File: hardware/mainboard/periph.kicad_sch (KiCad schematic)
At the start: 64 parts

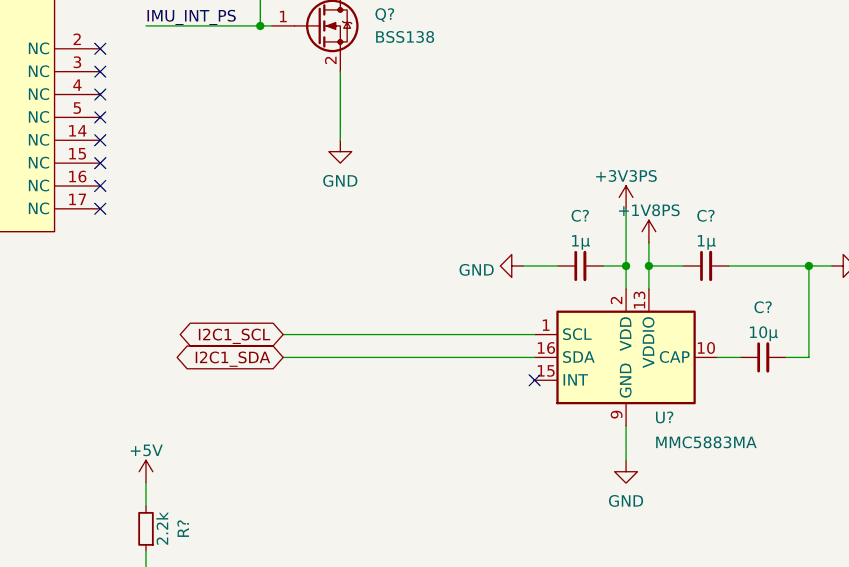
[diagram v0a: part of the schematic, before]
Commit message: Re-add USB-C PD control
Signed-off-by: gatecat <gatecat@ds0.me>
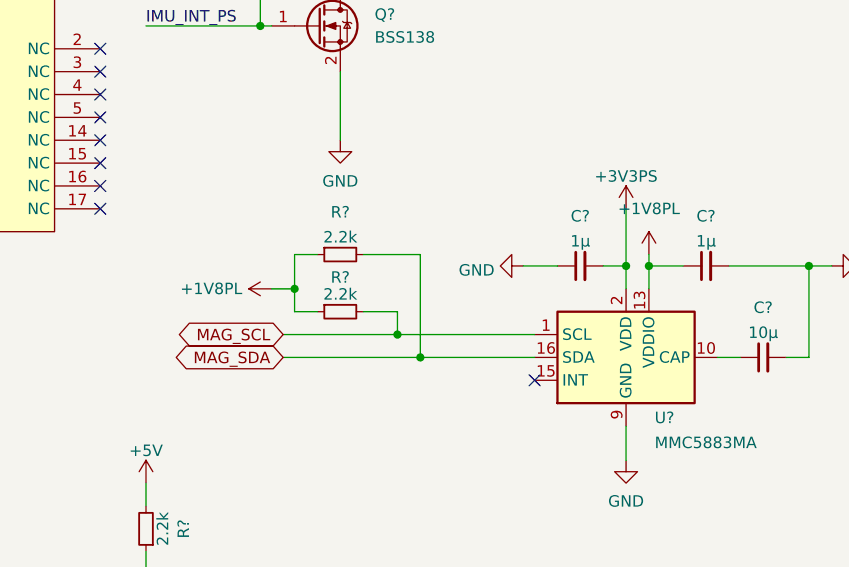
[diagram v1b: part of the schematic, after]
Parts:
- added R? (x2): 2.2k, Resistor_SMD:R_0402_1005Metric, symbol Device:R_Small
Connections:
- net +1V8PL: now also C?.1, U?.13 (VDDIO), R?.1, R?.1
- net +1V8PS: no longer C?.1, U?.13 (VDDIO)
- net I2C1_SCL: no longer U?.1 (SCL)
- net I2C1_SDA: no longer U?.16 (SDA)
- new net MAG_SCL: R?.2, U?.1 (SCL)
- new net MAG_SDA: R?.2, U?.16 (SDA)
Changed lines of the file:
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@@
   (junction (at 201.93 158.75) (diameter 0) (color 0 0 0 0)
   )
+  (junction (at 144.78 161.29) (diameter 0) (color 0 0 0 0)
+  )
   (junction (at 337.82 114.3) (diameter 0) (color 0 0 0 0)
   )
@@
   (junction (at 337.82 152.4) (diameter 0) (color 0 0 0 0)
   )
+  (junction (at 158.75 168.91) (diameter 0) (color 0 0 0 0)
+  )
   (junction (at 88.9 102.87) (diameter 0) (color 0 0 0 0)
   )
@@
   )
   (junction (at 233.68 140.97) (diameter 0) (color 0 0 0 0)
+  )
+  (junction (at 156.21 166.37) (diameter 0) (color 0 0 0 0)
   )
   (junction (at 391.16 66.04) (diameter 0) (color 0 0 0 0)
@@
     (stroke (width 0) (type default) (color 0 0 0 0))
   )
+  (wire (pts (xy 158.75 168.91) (xy 171.45 168.91))
+    (stroke (width 0) (type default) (color 0 0 0 0))
+  )
   (wire (pts (xy 176.53 45.72) (xy 190.5 45.72))
     (stroke (width 0) (type default) (color 0 0 0 0))
@@
     (stroke (width 0) (type default) (color 0 0 0 0))
   )
-  (wire (pts (xy 184.15 156.21) (xy 184.15 158.75))
+  (wire (pts (xy 184.15 157.48) (xy 184.15 158.75))
     (stroke (width 0) (type default) (color 0 0 0 0))
   )
@@
     (stroke (width 0) (type default) (color 0 0 0 0))
   )
+  (wire (pts (xy 156.21 166.37) (xy 171.45 166.37))
+    (stroke (width 0) (type default) (color 0 0 0 0))
+  )
   (wire (pts (xy 86.36 215.9) (xy 86.36 220.98))
     (stroke (width 0) (type default) (color 0 0 0 0))
@@
     (stroke (width 0) (type default) (color 0 0 0 0))
   )
+  (wire (pts (xy 144.78 161.29) (xy 144.78 157.48))
+    (stroke (width 0) (type default) (color 0 0 0 0))
+  )
   (wire (pts (xy 69.85 102.87) (xy 69.85 105.41))
     (stroke (width 0) (type default) (color 0 0 0 0))
@@
     (stroke (width 0) (type default) (color 0 0 0 0))
   )
+  (wire (pts (xy 152.4 157.48) (xy 158.75 157.48))
+    (stroke (width 0) (type default) (color 0 0 0 0))
+  )
   (wire (pts (xy 391.16 68.58) (xy 391.16 147.32))
     (stroke (width 0) (type default) (color 0 0 0 0))
@@
     (stroke (width 0) (type default) (color 0 0 0 0))
   )
-  (wire (pts (xy 143.51 168.91) (xy 171.45 168.91))
+  (wire (pts (xy 143.51 168.91) (xy 158.75 168.91))
     (stroke (width 0) (type default) (color 0 0 0 0))
   )
@@
     (stroke (width 0) (type default) (color 0 0 0 0))
   )
-  (wire (pts (xy 143.51 166.37) (xy 171.45 166.37))
+  (wire (pts (xy 143.51 166.37) (xy 156.21 166.37))
     (stroke (width 0) (type default) (color 0 0 0 0))
   )
@@
     (stroke (width 0) (type default) (color 0 0 0 0))
   )
+  (wire (pts (xy 152.4 163.83) (xy 156.21 163.83))
+    (stroke (width 0) (type default) (color 0 0 0 0))
+  )
   (wire (pts (xy 66.04 127) (xy 92.71 127))
     (stroke (width 0) (type default) (color 0 0 0 0))
@@
     (stroke (width 0) (type default) (color 0 0 0 0))
   )
+  (wire (pts (xy 144.78 161.29) (xy 144.78 163.83))
+    (stroke (width 0) (type default) (color 0 0 0 0))
+  )
   (wire (pts (xy 306.07 139.7) (xy 309.88 139.7))
     (stroke (width 0) (type default) (color 0 0 0 0))
@@
     (stroke (width 0) (type default) (color 0 0 0 0))
   )
+  (wire (pts (xy 156.21 163.83) (xy 156.21 166.37))
+    (stroke (width 0) (type default) (color 0 0 0 0))
+  )
   (wire (pts (xy 55.88 264.16) (xy 55.88 261.62))
     (stroke (width 0) (type default) (color 0 0 0 0))
@@
     (stroke (width 0) (type default) (color 0 0 0 0))
   )
+  (wire (pts (xy 142.24 161.29) (xy 144.78 161.29))
+    (stroke (width 0) (type default) (color 0 0 0 0))
+  )
   (wire (pts (xy 363.22 163.83) (xy 363.22 166.37))
     (stroke (width 0) (type default) (color 0 0 0 0))
@@
     (stroke (width 0) (type default) (color 0 0 0 0))
   )
+  (wire (pts (xy 144.78 163.83) (xy 147.32 163.83))
+    (stroke (width 0) (type default) (color 0 0 0 0))
+  )
   (wire (pts (xy 132.08 22.86) (xy 140.97 22.86))
     (stroke (width 0) (type default) (color 0 0 0 0))
@@
     (stroke (width 0) (type default) (color 0 0 0 0))
   )
+  (wire (pts (xy 158.75 157.48) (xy 158.75 168.91))
+    (stroke (width 0) (type default) (color 0 0 0 0))
+  )
   (wire (pts (xy 140.97 31.75) (xy 140.97 33.02))
     (stroke (width 0) (type default) (color 0 0 0 0))
@@
   )
   (wire (pts (xy 209.55 140.97) (xy 218.44 140.97))
+    (stroke (width 0) (type default) (color 0 0 0 0))
+  )
+  (wire (pts (xy 144.78 157.48) (xy 147.32 157.48))
     (stroke (width 0) (type default) (color 0 0 0 0))
   )
@@
     )
   )
-  (global_label "I2C1_SDA" (shape bidirectional) (at 143.51 168.91 180) (fields_autoplaced)
+  (global_label "MAG_SDA" (shape bidirectional) (at 143.51 168.91 180) (fields_autoplaced)
     (effects (font (size 1.27 1.27)) (justify right))
-    (property "Intersheet References" "${INTERSHEET_REFS}" (id 0) (at 132.2674 168.8306 0)
+    (property "Intersheet References" "${INTERSHEET_REFS}" (id 0) (at 132.7512 168.8306 0)
       (effects (font (size 1.27 1.27)) (justify right) hide)
     )
   )
-  (global_label "I2C1_SCL" (shape bidirectional) (at 143.51 166.37 180) (fields_autoplaced)
+  (global_label "MAG_SCL" (shape bidirectional) (at 143.51 166.37 180) (fields_autoplaced)
     (effects (font (size 1.27 1.27)) (justify right))
-    (property "Intersheet References" "${INTERSHEET_REFS}" (id 0) (at 132.3279 166.2906 0)
+    (property "Intersheet References" "${INTERSHEET_REFS}" (id 0) (at 132.8117 166.2906 0)
       (effects (font (size 1.27 1.27)) (justify right) hide)
     )
@@
     (pin "2")
   )
+  (symbol (lib_id "meowality:+1V8PL") (at 184.15 157.48 0) (unit 1)
+    (in_bom yes) (on_board yes) (fields_autoplaced)
+    (property "Reference" "#PWR?" (id 0) (at 184.15 161.29 0)
+      (effects (font (size 1.27 1.27)) hide)
+    )
+    (property "Value" "+1V8PL" (id 1) (at 184.15 152.4 0))
+    (property "Footprint" "" (id 2) (at 184.15 157.48 0)
+      (effects (font (size 1.27 1.27)) hide)
+    )
+    (property "Datasheet" "" (id 3) (at 184.15 157.48 0)
+      (effects (font (size 1.27 1.27)) hide)
+    )
+    (pin "1")
+  )
   (symbol (lib_id "Device:C_Small") (at 312.42 139.7 90) (unit 1)
     (in_bom yes) (on_board yes)
@@
     (pin "2")
   )
+  (symbol (lib_id "meowality:+1V8PL") (at 142.24 161.29 90) (unit 1)
+    (in_bom yes) (on_board yes)
+    (property "Reference" "#PWR?" (id 0) (at 146.05 161.29 0)
+      (effects (font (size 1.27 1.27)) hide)
+    )
+    (property "Value" "+1V8PL" (id 1) (at 132.08 161.29 90)
+      (effects (font (size 1.27 1.27)) (justify right))
+    )
+    (property "Footprint" "" (id 2) (at 142.24 161.29 0)
+      (effects (font (size 1.27 1.27)) hide)
+    )
+    (property "Datasheet" "" (id 3) (at 142.24 161.29 0)
+      (effects (font (size 1.27 1.27)) hide)
+    )
+    (pin "1")
+  )
   (symbol (lib_id "Device:C_Small") (at 209.55 124.46 0) (unit 1)
     (in_bom yes) (on_board yes)
@@
     (pin "3")
     (pin "4")
+  )
+  (symbol (lib_id "Device:R_Small") (at 149.86 163.83 90) (mirror x) (unit 1)
+    (in_bom yes) (on_board yes)
+    (property "Reference" "R?" (id 0) (at 149.86 160.02 90))
+    (property "Value" "2.2k" (id 1) (at 149.86 161.902 90))
+    (property "Footprint" "Resistor_SMD:R_0402_1005Metric" (id 2) (at 149.86 163.83 0)
+      (effects (font (size 1.27 1.27)) hide)
+    )
+    (property "Datasheet" "~" (id 3) (at 149.86 163.83 0)
+      (effects (font (size 1.27 1.27)) hide)
+    )
+    (pin "1")
+    (pin "2")
   )
   (symbol (lib_id "power:GND") (at 138.43 269.24 0) (unit 1)
@@
     (pin "2")
   )
+  (symbol (lib_id "Device:R_Small") (at 149.86 157.48 90) (mirror x) (unit 1)
+    (in_bom yes) (on_board yes) (fields_autoplaced)
+    (property "Reference" "R?" (id 0) (at 149.86 152.7769 90))
+    (property "Value" "2.2k" (id 1) (at 149.86 155.552 90))
+    (property "Footprint" "Resistor_SMD:R_0402_1005Metric" (id 2) (at 149.86 157.48 0)
+      (effects (font (size 1.27 1.27)) hide)
+    )
+    (property "Datasheet" "~" (id 3) (at 149.86 157.48 0)
+      (effects (font (size 1.27 1.27)) hide)
+    )
+    (pin "1")
+    (pin "2")
+  )
   (symbol (lib_id "Transistor_FET:BSS138") (at 83.82 205.74 0) (unit 1)
     (in_bom yes) (on_board yes) (fields_autoplaced)
@@
     (pin "2")
   )
-  (symbol (lib_id "meowality:+1V8PS") (at 184.15 156.21 0) (unit 1)
-    (in_bom yes) (on_board yes) (fields_autoplaced)
-    (property "Reference" "#PWR?" (id 0) (at 184.15 160.02 0)
-      (effects (font (size 1.27 1.27)) hide)
-    )
-    (property "Value" "+1V8PS" (id 1) (at 184.15 152.6055 0))
-    (property "Footprint" "" (id 2) (at 184.15 156.21 0)
-      (effects (font (size 1.27 1.27)) hide)
-    )
-    (property "Datasheet" "" (id 3) (at 184.15 156.21 0)
-      (effects (font (size 1.27 1.27)) hide)
-    )
-    (pin "1")
-  )
   (symbol (lib_id "Device:R_Small") (at 45.72 187.96 180) (unit 1)

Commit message: ERC fixes
Signed-off-by: gatecat <gatecat@ds0.me>
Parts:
- added D10, D11, D8, D9: PESD3V3L4UF, Package_TO_SOT_SMD:SOT-886, symbol Power_Protection:PESD3V3L4UF
- added R41: DNP, symbol Device:R_Small
- added R42, R43, R44, R45: 10k, symbol Device:R_Small
- added SW2, SW3, SW4, SW5, SW6: SW_Push, symbol Switch:SW_Push
- added U21: 74LVC2T45DC, Package_SO:VSSOP-8_2.3x2mm_P0.5mm, symbol Logic_LevelTranslator:74LVC2T45DC
- gave numbers to parts that had none: 66
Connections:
- net +1V8PS: now also R41.1, R42.1, R43.1, R44.1, R45.1, U21.8 (VCCB)
- net +3V3PS: now also U21.1 (VCCA)
- net GND: now also D10.2 (A), D10.5 (A), D11.2 (A), D11.5 (A), D8.2 (A), D8.5 (A), D9.2 (A), D9.5 (A), SW2.2, SW3.2, SW4.2, SW5.2, SW6.2, U21.4 (GND), U21.5 (DIR)
- net PERST_3V3: now also U21.2 (1A)
- new net BTN0: D8.1 (K1), R42.2, SW3.1
- new net BTN1: D9.1 (K1), R43.2, SW4.1
- new net BTN2: D10.1 (K1), R44.2, SW5.1
- new net BTN3: D11.1 (K1), R45.2, SW6.1
- new net DP_HPD: U21.6 (2B)
- new net DP_HPD_3V3: U21.3 (2A)
- new net PCIE_~{PERST}: U21.7 (1B)
- new net SYS_RESET: R41.2, SW2.1
